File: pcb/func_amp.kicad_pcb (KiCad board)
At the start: 2 copper layers, 86 x 50 mm, 28 parts, among them J1 PWR, J2 IN, J3 LOAD, U1 L7815, U2 L7915, U3 TDA2030

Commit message: update footprints
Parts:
- added C1: 3300uF, Capacitor_THT:CP_Radial_D18.0mm_P7.50mm, F.Cu at (158.6, 17.8)
- added C19: 220p, Capacitor_THT:C_Rect_L7.2mm_W4.5mm_P5.00mm_FKS2_FKP2_MKS2_MKP2, F.Cu at (153.9, 62.0)
- added C2: 3300uF, Capacitor_THT:CP_Radial_D18.0mm_P7.50mm, F.Cu at (158.6, 37.3)
- added C3: 3300uF, Capacitor_THT:CP_Radial_D18.0mm_P7.50mm, F.Cu at (178.7, 17.8)
- added C4: 3300uF, Capacitor_THT:CP_Radial_D18.0mm_P7.50mm, F.Cu at (178.7, 37.3)
- added D1: KBP10G, Diode_THT:Diode_Bridge_Vishay_KBPM, F.Cu at (171.8, 50.3)
- added NT1: Net-Tie_3_Tee, NetTie:NetTie-3_SMD_Pad2.0mm, F.Cu at (177.6, 71.7)
- added P1: AC-01B, TerminalBlock_Phoenix:TerminalBlock_Phoenix_MKDS-1,5-3-5.08_1x03_P5.08mm_Horizontal, F.Cu at (155.6, 53.3)
- added R11: 1k, Resistor_THT:R_Axial_DIN0207_L6.3mm_D2.5mm_P10.16mm_Horizontal, F.Cu at (173.4, 63.9)
- added R12: 1k, Resistor_THT:R_Axial_DIN0207_L6.3mm_D2.5mm_P10.16mm_Horizontal, F.Cu at (173.4, 67.9)
- added R7: 5k2, Resistor_THT:R_Axial_DIN0207_L6.3mm_D2.5mm_P10.16mm_Horizontal, F.Cu at (173.4, 55.8)
- added R8: 5k2, Resistor_THT:R_Axial_DIN0207_L6.3mm_D2.5mm_P10.16mm_Horizontal, F.Cu at (173.4, 59.8)
- added T1: ST-6-20, pl_Transformer:ST-6-20, F.Cu at (127.6, 37.1)
- C10, C9: footprint Capacitor_THT:C_Rect_L7.0mm_W3.5mm_P5.00mm -> Capacitor_THT:C_Rect_L13.0mm_W4.0mm_P10.00mm_FKS3_FKP3_MKS4
- C11: footprint Capacitor_THT:C_Rect_L10.3mm_W5.7mm_P7.50mm_MKS4 -> Capacitor_THT:C_Rect_L13.0mm_W8.0mm_P10.00mm_FKS3_FKP3_MKS4
- C5: value 1u -> 2.2u; footprint Capacitor_THT:CP_Radial_D5.0mm_P2.50mm -> Capacitor_THT:C_Rect_L31.5mm_W11.0mm_P27.50mm_MKS4
- C6: value 22u -> 220u; footprint Capacitor_THT:CP_Radial_D5.0mm_P2.50mm -> Capacitor_THT:CP_Radial_D8.0mm_P3.80mm
- C7, C8: footprint Capacitor_THT:CP_Radial_D6.3mm_P2.50mm -> Capacitor_THT:CP_Radial_D8.0mm_P3.80mm
- J2: footprint Connector_Coaxial:BNC_TEConnectivity_1478204_Vertical -> Connector_Coaxial:BNC_Amphenol_B6252HB-NPP3G-50_Horizontal
- R1: value 22k -> 21k
- R2: value 680R -> 1k
- R4: value 1R -> 10R; footprint Resistor_THT:R_Axial_DIN0207_L6.3mm_D2.5mm_P10.16mm_Horizontal -> Resistor_THT:R_Axial_DIN0411_L9.9mm_D3.6mm_P15.24mm_Horizontal
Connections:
- C10 pad 1: GND -> GNDPWR
- C10 pad 2: -15V -> -V
- C11 pad 2: GND -> GNDPWR
- C6 pad 2: GND -> GNDS
- C7 pad 1: +15V -> +V
- C7 pad 2: GND -> GNDPWR
- C8 pad 1: GND -> GNDPWR
- C8 pad 2: -15V -> -V
- C9 pad 1: +15V -> +V
- C9 pad 2: GND -> GNDPWR
- D3 pad 1: +15V -> +V
- D3 pad 2: Net-(C12-Pad1) -> Net-(D3-Pad2)
- D4 pad 1: Net-(C12-Pad1) -> Net-(D3-Pad2)
- D4 pad 2: -15V -> -V
- J2 pad 2: GND -> GNDS
- J3 pad 2: Net-(C12-Pad1) -> Net-(D3-Pad2)
- R1 pad 1: Net-(C5-Pad2) -> Net-(R1-Pad1)
- R1 pad 2: GND -> GNDS
- R3 pad 1: Net-(C12-Pad1) -> Net-(D3-Pad2)
- R4 pad 1: Net-(C12-Pad1) -> Net-(D3-Pad2)
- R6 pad 2: GND -> GNDS
- U3 pad 1: Net-(C5-Pad2) -> Net-(C19-Pad1)
- U3 pad 3: -15V -> -V
- U3 pad 4: Net-(C12-Pad1) -> Net-(D3-Pad2)
- U3 pad 5: +15V -> +V

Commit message: pcb layout
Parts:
- removed the C1 at (158.6, 17.8)
- removed the C1 at (175.0, 100.0)
- removed C12: 2.2n, Capacitor_THT:C_Rect_L7.0mm_W3.5mm_P5.00mm
- removed the C2 at (158.6, 37.3)
- removed the C2 at (175.8, 117.0)
- removed the C3 at (178.7, 17.8)
- removed the C3 at (175.0, 93.0)
- removed the C4 at (178.7, 37.3)
- removed the C4 at (177.0, 109.0)
- removed the D1 at (171.8, 50.3)
- removed the D1 at (160.0, 92.0)
- removed D2: 1N4001, Diode_THT:D_DO-41_SOD81_P10.16mm_Horizontal
- removed NT1: Net-Tie_3_Tee, NetTie:NetTie-3_SMD_Pad2.0mm
- removed P1: AC-01B, TerminalBlock_Phoenix:TerminalBlock_Phoenix_MKDS-1,5-3-5.08_1x03_P5.08mm_Horizontal
- removed R5: 3R2, Resistor_THT:R_Axial_DIN0207_L6.3mm_D2.5mm_P10.16mm_Horizontal
- removed U1: L7815, Package_TO_SOT_THT:TO-220-3_Vertical
- removed U2: L7915, Package_TO_SOT_THT:TO-220-3_Vertical
- added C1: 3300uF, Capacitor_THT:CP_Radial_D18.0mm_P7.50mm, F.Cu at (135.0, 62.1)
- added C2: 3300uF, Capacitor_THT:CP_Radial_D18.0mm_P7.50mm, F.Cu at (135.0, 43.0)
- added C3: 3300uF, Capacitor_THT:CP_Radial_D18.0mm_P7.50mm, F.Cu at (154.5, 62.1)
- added C4: 3300uF, Capacitor_THT:CP_Radial_D18.0mm_P7.50mm, F.Cu at (154.5, 43.0)
- added D1: KBP10G, Diode_THT:Diode_Bridge_Vishay_KBPM, F.Cu at (118.0, 62.1)
- added H1: MountingHole, MountingHole:MountingHole_3.2mm_M3, F.Cu at (53.5, 28.5)
- added H2: MountingHole, MountingHole:MountingHole_3.2mm_M3, F.Cu at (53.5, 151.5)
- added H3: MountingHole, MountingHole:MountingHole_3.2mm_M3, F.Cu at (176.5, 151.5)
- added H4: MountingHole, MountingHole:MountingHole_3.2mm_M3, F.Cu at (176.5, 28.5)
- added HS1: Heatsink, pl_heatsink:random_psu_heatsink, F.Cu at (74.0, 96.7)
- added J10: GNDS, pl_connector:TE_0.25in_spade_63824-1, F.Cu at (145.0, 30.0)
- added J11: GND, pl_connector:TE_0.25in_spade_63824-1, F.Cu at (158.3, 102.5)
- added J12: GNDPWR, pl_connector:TE_0.25in_spade_63824-1, F.Cu at (149.0, 128.0)
- added J13: GNDPWR, pl_connector:TE_0.25in_spade_63824-1, F.Cu at (157.5, 30.0)
- added J4: IN, pl_connector:TE_0.25in_spade_63824-1, F.Cu at (71.5, 135.9)
- added J5: GNDS, pl_connector:TE_0.25in_spade_63824-1, F.Cu at (66.5, 150.3)
- added J6: OUT, pl_connector:TE_0.25in_spade_63824-1, F.Cu at (148.0, 108.1)
- added J7: GND, pl_connector:TE_0.25in_spade_63824-1, F.Cu at (158.3, 108.1)
- added J8: GNDS, pl_connector:TE_0.25in_spade_63824-1, F.Cu at (77.5, 150.0)
- added J9: GND, pl_connector:TE_0.25in_spade_63824-1, F.Cu at (132.5, 30.0)
- J1: value PWR -> L; footprint TerminalBlock_Phoenix:TerminalBlock_Phoenix_MKDS-1,5-3-5.08_1x03_P5.08mm_Horizontal -> pl_connector:TE_0.25in_spade_63824-1
- J2: value IN -> N; footprint Connector_Coaxial:BNC_Amphenol_B6252HB-NPP3G-50_Horizontal -> pl_connector:TE_0.25in_spade_63824-1
- J3: value LOAD -> G; footprint TerminalBlock_Phoenix:TerminalBlock_Phoenix_MKDS-1,5-2-5.08_1x02_P5.08mm_Horizontal -> pl_connector:TE_0.25in_spade_63824-1
- moved J1 137.8 mm to (53.0, 71.4)
- moved J2 93.2 mm to (53.0, 40.8), turned to 90 degrees
- moved R11 91.0 mm to (118.2, 136.2), turned to 270 degrees
- moved J3 82.0 mm to (120.0, 30.0), turned to 180 degrees
- moved R12 80.3 mm to (114.8, 122.7), turned to 270 degrees
- moved C19 69.6 mm to (120.0, 122.7), turned to 270 degrees
- moved C5 51.7 mm to (86.1, 144.7)
- moved T1 45.4 mm to (86.4, 56.1)
- moved R6 44.6 mm to (80.2, 135.9)
- moved C8 39.7 mm to (138.7, 143.0)
- moved C10 38.0 mm to (127.7, 136.8)
- moved C7 37.2 mm to (138.7, 133.3)
- moved C6 36.7 mm to (97.4, 132.2)
- moved R3 36.5 mm to (100.8, 122.7)
- moved R2 36.4 mm to (110.9, 127.7)
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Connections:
- J1 pad 1: /-V -> /L
- J2 pad 1: Net-(C5-Pad1) -> /N
- J3 pad 1: GND -> Earth
- R7 pad 2: GNDPWR -> Earth
- R8 pad 1: GNDPWR -> Earth
- T1 pad 6: GNDPWR -> Earth
- T1 pad 7: GNDPWR -> Earth
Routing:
- net Net-(C12-Pad1): track 113.2 -> 0.00 mm
- net -15V: track 73.5 -> 0.00 mm
- net +15V: track 60.1 -> 0.00 mm
- net Net-(D3-Pad2): track 0.00 -> 59.7 mm
- net -V: track 0.00 -> 51.0 mm
- net Net-(C5-Pad1): track 42.0 -> 11.2 mm
- net +V: track 0.00 -> 28.1 mm
- net Net-(C5-Pad2): track 33.2 -> 5.35 mm
- net Net-(D1-Pad3): track 0.00 -> 20.0 mm
- net Net-(D1-Pad2): track 0.00 -> 19.5 mm
- net /+V: track 17.7 -> 0.00 mm
- net /-V: track 16.5 -> 0.00 mm
- net Net-(C19-Pad1): track 0.00 -> 15.3 mm
- net Net-(R1-Pad1): track 0.00 -> 6.84 mm
- net Net-(C12-Pad2): track 4.00 -> 0.00 mm
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- added copper zone on B.Cu, net +V
- added copper zone on B.Cu, net -V
- added copper zone on B.Cu, net /L
- added copper zone on B.Cu, net /N
- added copper zone on B.Cu, net Earth
- removed copper zone on B.Cu, net GND
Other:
- board size 86 x 50 mm -> 130 x 130 mm
- board text removed: "+"
- board text removed: "-"

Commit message: Update func_amp.kicad_pcb
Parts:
- moved J8 30.0 mm to (70.2, 120.9)
- moved J5 22.2 mm to (70.2, 128.4)
- moved J12 14.0 mm to (163.0, 128.0)
- moved J11 10.5 mm to (155.0, 92.5)
- moved C11 10.1 mm to (150.0, 118.0)
- moved C7 9.59 mm to (140.0, 123.8)
- moved J7 8.75 mm to (155.0, 100.0)
- moved J6 7.03 mm to (155.0, 107.5)
- moved J4 1.30 mm to (70.2, 135.9)
- moved D4 0.55 mm to (128.3, 117.7)
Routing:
- net -V: track 51.0 -> 0.00 mm
- net Net-(D3-Pad2): track 59.7 -> 85.4 mm
- net +V: track 28.1 -> 12.1 mm
- net Net-(C5-Pad1): track 11.2 -> 23.8 mm
- net Net-(C11-Pad1): track 10.1 -> 5.85 mm
- added copper zone on B.Cu, net (none)
- added copper zone on B.Cu, net GND
- added copper zone on B.Cu, net GNDPWR
- added copper zone on B.Cu, net GNDS
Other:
- outline, holes or cut-outs redrawn

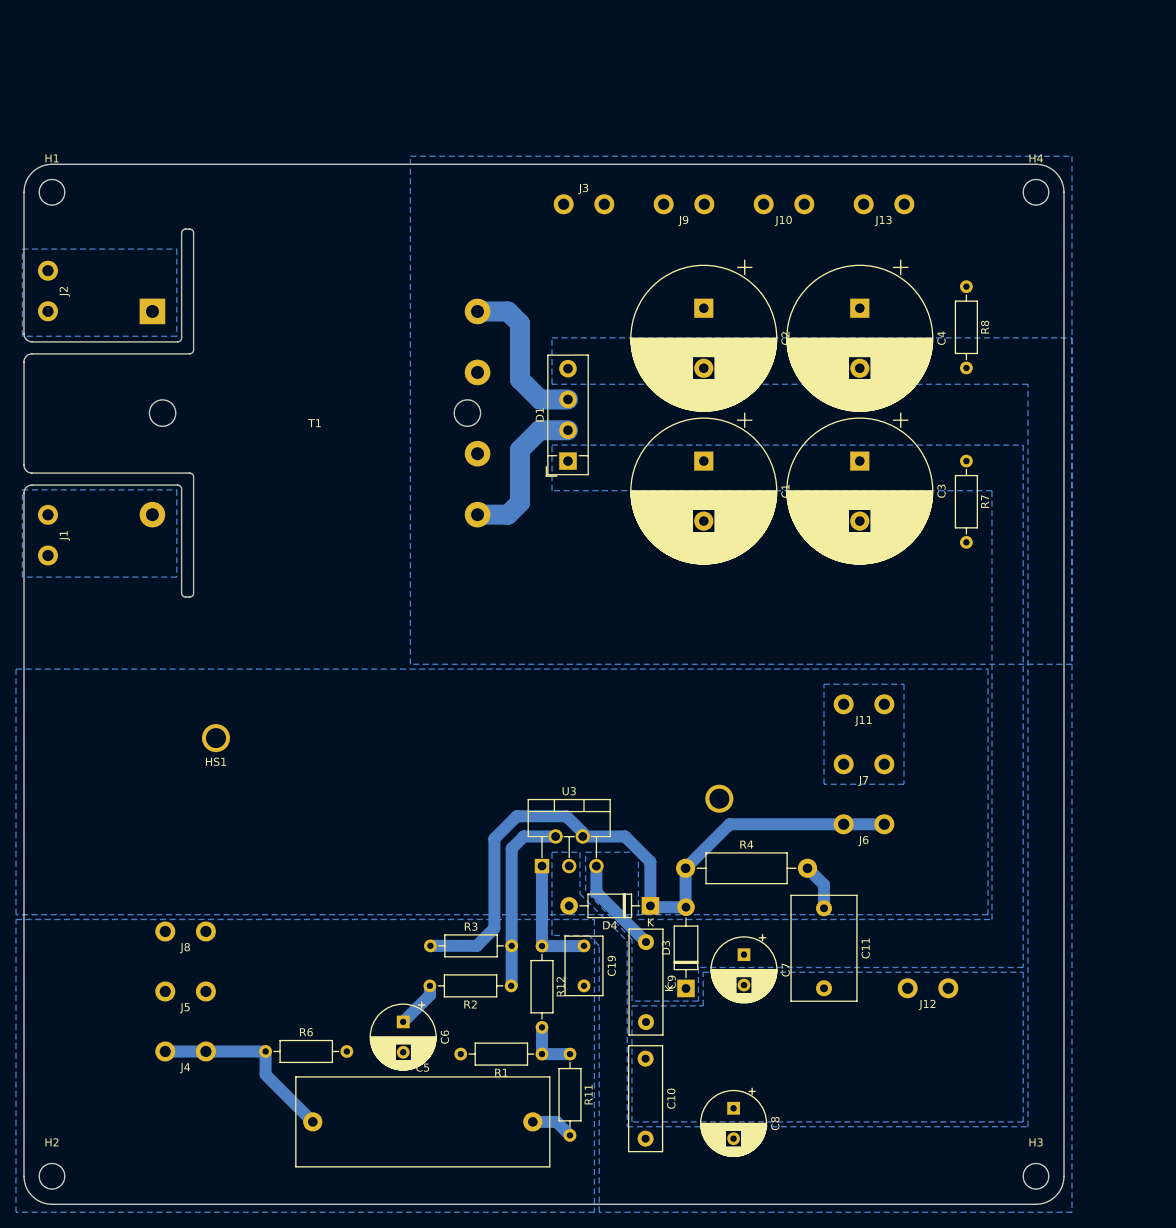
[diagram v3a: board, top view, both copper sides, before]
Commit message: update to KiCAD V6
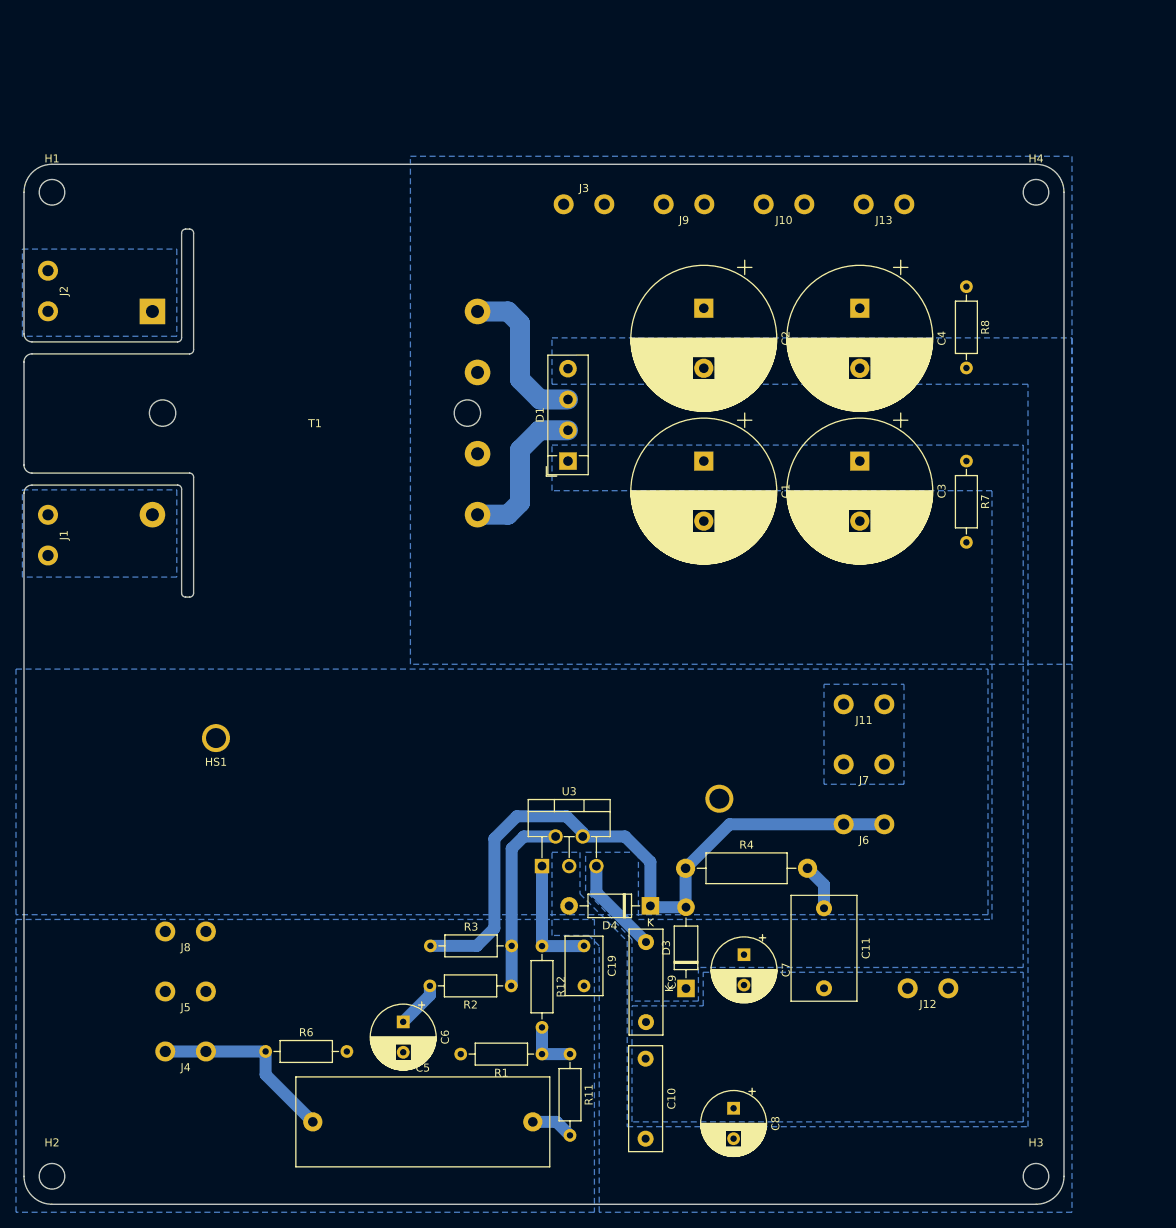
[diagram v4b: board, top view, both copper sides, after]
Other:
- net class Default removed
